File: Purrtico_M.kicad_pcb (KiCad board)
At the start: 2 copper layers, 100 x 60 mm, 123 parts, among them J1 Conn_02x05_Odd_Even, J2 Conn_01x02, J4 Conn_01x02, U1 OPA1679, U2 OPA1679, U3 OPA1679

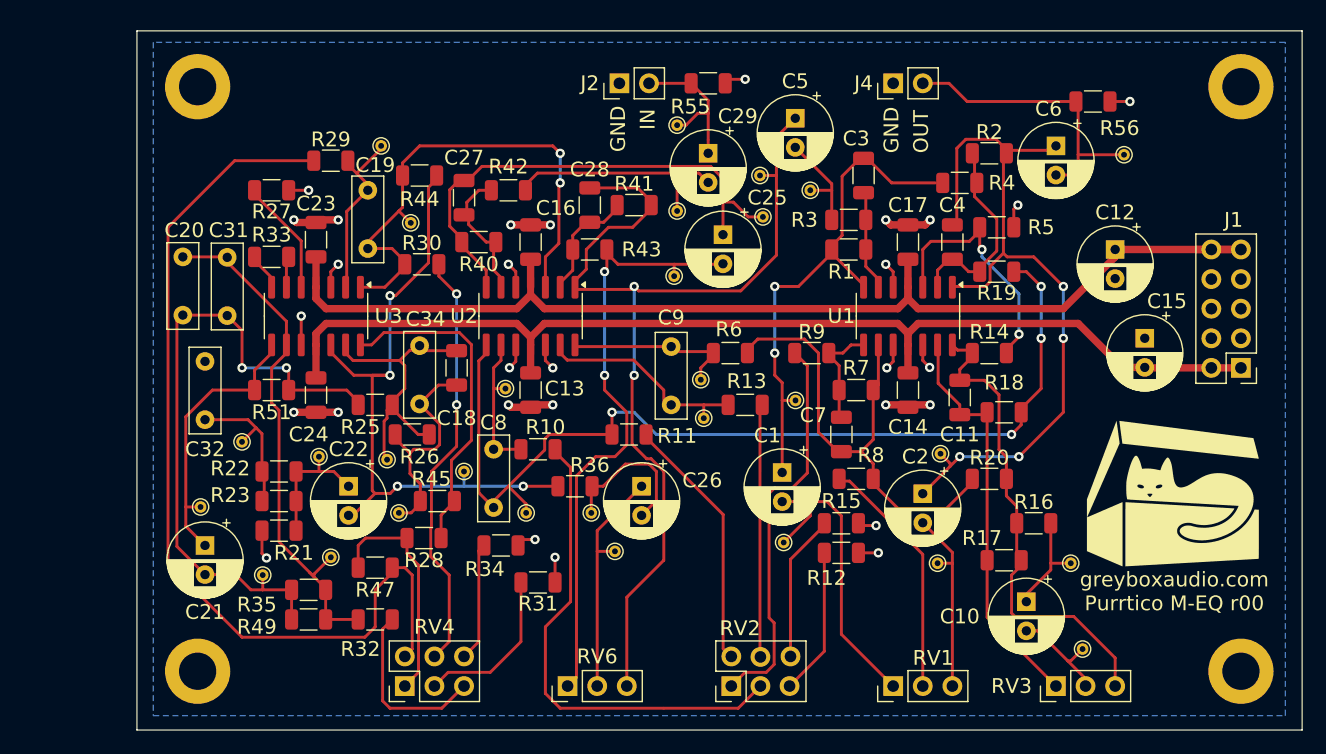
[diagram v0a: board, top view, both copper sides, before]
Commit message: first update after testing
shelving circuit not working for whatever reason :/
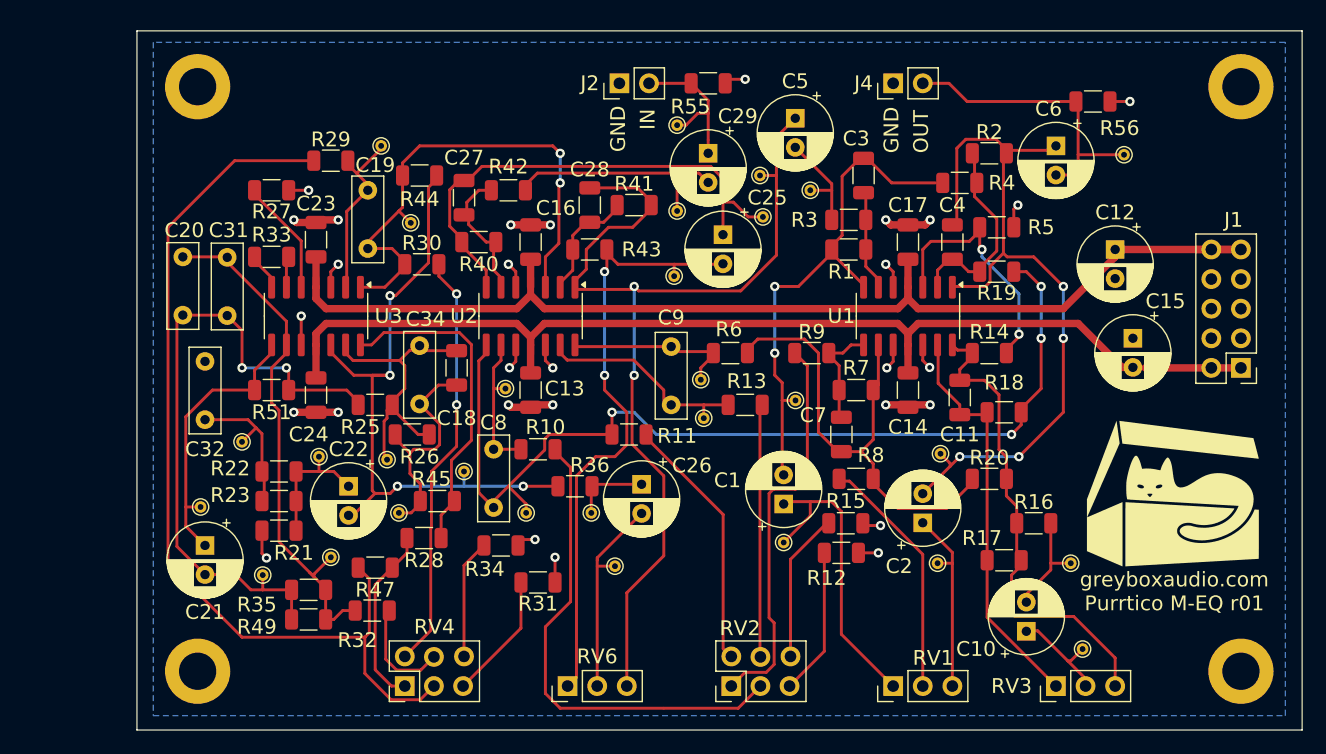
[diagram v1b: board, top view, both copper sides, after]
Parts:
- C8, C9: value 5n6 -> 56n
- RV1, RV6: value 4k7 -> 5k
- moved C1 2.71 mm to (143.0, 70.1), turned to 90 degrees
- moved C10 2.54 mm to (163.8, 81.0), turned to 90 degrees
- moved C2 2.50 mm to (154.9, 71.7), turned to 90 degrees
- moved TP5 1.27 mm to (128.5, 75.4)
- moved C15 1.02 mm to (173.0, 55.9)
- moved R32 0.80 mm to (107.7, 79.2)
- moved R15 0.38 mm to (148.3, 71.8)
- moved C26 0.17 mm to (130.8, 68.4)
- turned R47 to 0 degrees
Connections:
- C3 pad 2: Net-(C1-Pad1) -> Net-(C1-Pad2)
- C4 pad 2: Net-(C2-Pad1) -> Net-(C2-Pad2)
- C6 pad 1: Net-(C2-Pad1) -> Net-(C2-Pad2)
- R1 pad 2: Net-(C1-Pad1) -> Net-(C1-Pad2)
- R16 pad 2: Net-(C10-Pad1) -> Net-(C10-Pad2)
- R2 pad 2: Net-(C2-Pad1) -> Net-(C2-Pad2)
- R36 pad 2: Net-(C26-Pad2) -> Net-(C26-Pad1)
- R4 pad 1: Net-(C1-Pad1) -> Net-(C1-Pad2)
- RV1 pad 1: Net-(C1-Pad2) -> Net-(C1-Pad1)
- RV1 pad 3: Net-(C2-Pad2) -> Net-(C2-Pad1)
- RV3 pad 2: Net-(C10-Pad2) -> Net-(C10-Pad1)
- RV6 pad 2: Net-(C26-Pad1) -> Net-(C26-Pad2)
- TP10 pad 1: Net-(C1-Pad2) -> Net-(C1-Pad1)
- TP11 pad 1: Net-(C2-Pad2) -> Net-(C2-Pad1)
- TP12 pad 1: Net-(C2-Pad1) -> Net-(C2-Pad2)
- TP18 pad 1: Net-(C10-Pad2) -> Net-(C10-Pad1)
- TP19 pad 1: Net-(C10-Pad1) -> Net-(C10-Pad2)
- TP5 pad 1: Net-(C26-Pad1) -> Net-(C26-Pad2)
- TP6 pad 1: Net-(C26-Pad2) -> Net-(C26-Pad1)
- TP9 pad 1: Net-(C1-Pad1) -> Net-(C1-Pad2)
- U1 pad 1: Net-(C2-Pad1) -> Net-(C2-Pad2)
- U1 pad 7: Net-(C1-Pad1) -> Net-(C1-Pad2)
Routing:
- net Net-(C2-Pad2): track 16.3 -> 62.8 mm, vias 0 -> 4
- net Net-(C2-Pad1): track 62.8 -> 16.3 mm, vias 4 -> 0
- net Net-(C1-Pad2): track 26.5 -> 42.3 mm, vias 0 -> 2
- net Net-(C1-Pad1): track 42.3 -> 26.7 mm, vias 2 -> 0
- net Net-(C26-Pad1): track 20.2 -> 6.63 mm
- net Net-(R32-Pad2): track 15.4 -> 9.30 mm
- net Net-(C26-Pad2): track 13.5 -> 18.3 mm
- net Net-(R28-Pad1): track 20.0 -> 15.6 mm
- net Net-(R31-Pad2): track 14.1 -> 10.9 mm
- net Net-(R29-Pad1): track 78.9 -> 80.2 mm
- net -15V: track 93.2 -> 92.2 mm
- net Net-(C10-Pad2): track 8.47 -> 9.31 mm
- net Net-(C10-Pad1): track 9.31 -> 8.47 mm
- net Net-(R34-Pad2): track 10.2 -> 10.9 mm
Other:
- board text added: "greyboxaudio.com Purrtico M-EQ r01"
- board text removed: "greyboxaudio.com Purrtico M-EQ r00"

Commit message: update schematic
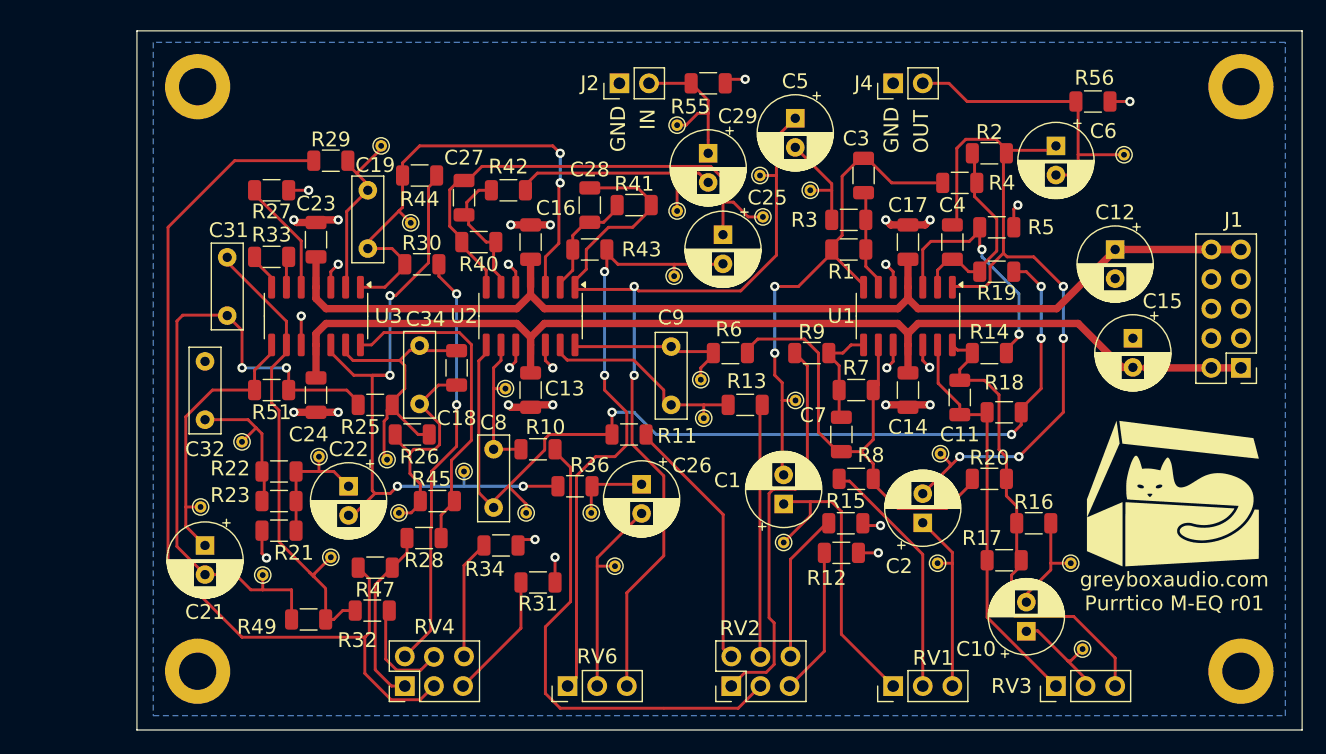
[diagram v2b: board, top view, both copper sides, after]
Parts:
- removed C20: 470n, Capacitor_THT:C_Rect_L7.2mm_W2.5mm_P5.00mm_FKS2_FKP2_MKS2_MKP2
- removed R35: 1M, Resistor_SMD:R_1206_3216Metric
- C31: value 470n -> 4n7
- R12, R15: value 390R -> 2k7
- R28, R30: value 100R -> 3k9
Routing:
- net Net-(U3C--): track 43.8 -> 40.0 mm
- net Net-(C10-Pad2): track 9.31 -> 8.68 mm
- net Net-(R34-Pad2): track 10.9 -> 10.2 mm

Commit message: update pcb
added 470p cap as MLCC, removed two mounting holes to create space for wider potentiometer spacing, swapped rows of RV6 to enable the use of a single gang potentiometer for the high shelf
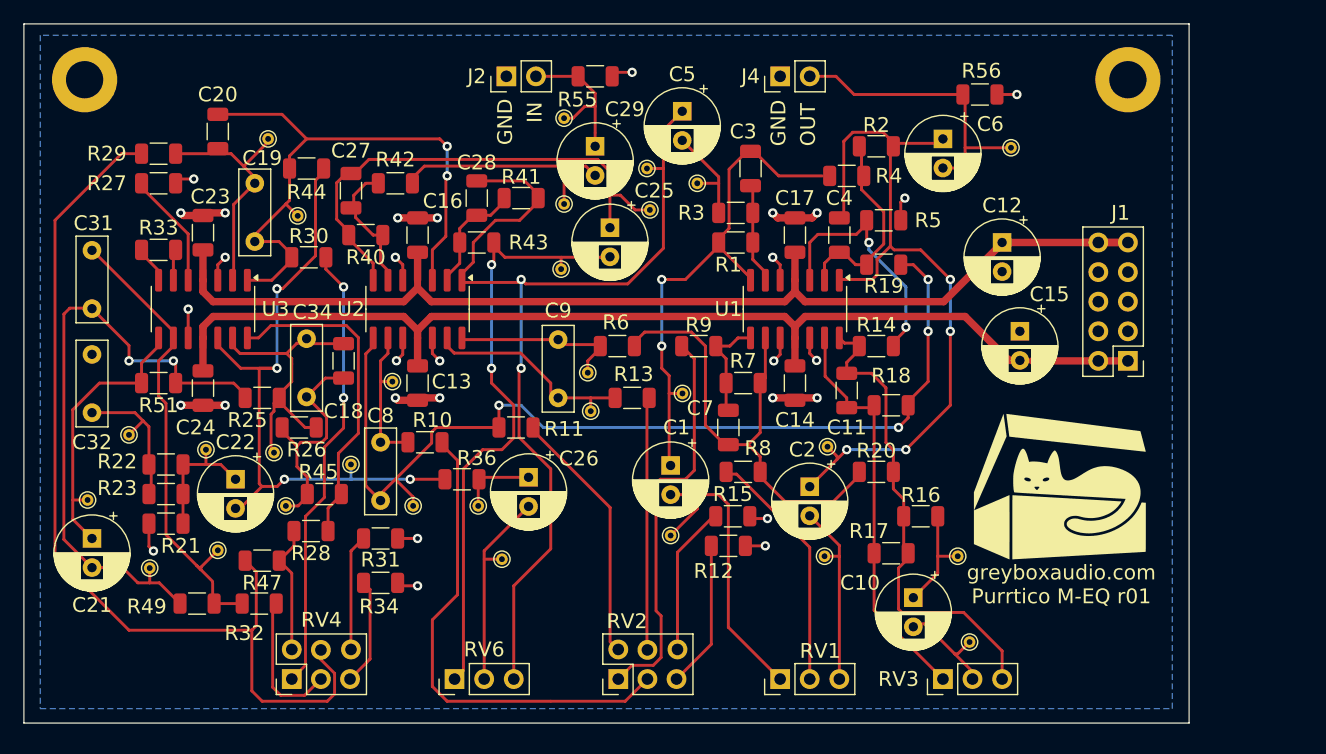
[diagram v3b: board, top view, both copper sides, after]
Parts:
- removed H3, H4: MountingHole, MountingHole:MountingHole_3.2mm_M3_DIN965_Pad
- added C20: 470p, Capacitor_SMD:C_1206_3216Metric, F.Cu at (94.4, 38.1)
- moved R29 14.8 mm to (89.4, 40.0)
- moved R31 14.0 mm to (108.4, 73.1)
- moved C31 11.6 mm to (83.6, 48.3)
- moved R34 10.8 mm to (108.4, 76.9)
- moved C1 10.2 mm to (133.3, 66.8), turned to -90 degrees
- moved C2 10.2 mm to (145.2, 68.6), turned to -90 degrees
- moved C10 10.1 mm to (154.1, 78.1), turned to -90 degrees
- moved C11 9.72 mm to (148.4, 60.4)
- moved C3 9.72 mm to (140.2, 41.3)
- moved C6 9.72 mm to (156.7, 38.8)
- moved C7 9.72 mm to (138.3, 63.5)
- moved H2 9.72 mm to (172.5, 33.7)
- moved J1 9.72 mm to (172.5, 57.8)
- moved J4 9.72 mm to (142.7, 33.4)
- moved R1 9.72 mm to (138.9, 47.7)
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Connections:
- C3 pad 2: Net-(C1-Pad2) -> Net-(C1-Pad1)
- C4 pad 2: Net-(C2-Pad2) -> Net-(C2-Pad1)
- C6 pad 1: Net-(C2-Pad2) -> Net-(C2-Pad1)
- R1 pad 2: Net-(C1-Pad2) -> Net-(C1-Pad1)
- R16 pad 2: Net-(C10-Pad2) -> Net-(C10-Pad1)
- R2 pad 2: Net-(C2-Pad2) -> Net-(C2-Pad1)
- R4 pad 1: Net-(C1-Pad2) -> Net-(C1-Pad1)
- RV1 pad 1: Net-(C1-Pad1) -> Net-(C1-Pad2)
- RV1 pad 3: Net-(C2-Pad1) -> Net-(C2-Pad2)
- RV3 pad 2: Net-(C10-Pad1) -> Net-(C10-Pad2)
- RV4 pad 1: Net-(R28-Pad1) -> Net-(R30-Pad2)
- RV4 pad 2: Net-(R29-Pad1) -> Net-(R32-Pad2)
- RV4 pad 3: Net-(R31-Pad2) -> Net-(R34-Pad2)
- RV4 pad 4: Net-(R30-Pad2) -> Net-(R28-Pad1)
- RV4 pad 5: Net-(R32-Pad2) -> Net-(R29-Pad1)
- RV4 pad 6: Net-(R34-Pad2) -> Net-(R31-Pad2)
- TP10 pad 1: Net-(C1-Pad1) -> Net-(C1-Pad2)
- TP11 pad 1: Net-(C2-Pad1) -> Net-(C2-Pad2)
- TP12 pad 1: Net-(C2-Pad2) -> Net-(C2-Pad1)
- TP18 pad 1: Net-(C10-Pad1) -> Net-(C10-Pad2)
- TP19 pad 1: Net-(C10-Pad2) -> Net-(C10-Pad1)
- TP9 pad 1: Net-(C1-Pad2) -> Net-(C1-Pad1)
- U1 pad 1: Net-(C2-Pad2) -> Net-(C2-Pad1)
- U1 pad 7: Net-(C1-Pad2) -> Net-(C1-Pad1)
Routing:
- net Net-(C2-Pad2): track 62.8 -> 16.3 mm, vias 4 -> 0
- net Net-(C2-Pad1): track 16.3 -> 62.8 mm, vias 0 -> 4
- net Net-(C1-Pad1): track 26.7 -> 42.3 mm, vias 0 -> 2
- net Net-(C1-Pad2): track 42.3 -> 26.7 mm, vias 2 -> 0
- net Net-(U2A-+): track 44.0 -> 52.5 mm
- net Net-(U3A--): track 14.4 -> 19.6 mm
- net Net-(R28-Pad1): track 15.6 -> 11.1 mm
- net Net-(R32-Pad2): track 8.86 -> 11.9 mm
- net Net-(C21-Pad2): track 56.2 -> 53.4 mm
- net Net-(R30-Pad2): track 36.1 -> 38.7 mm
- net Net-(R29-Pad1): track 80.2 -> 81.9 mm
- net Net-(C10-Pad1): track 8.47 -> 9.57 mm
- net Net-(R34-Pad2): track 10.2 -> 9.20 mm
- net Net-(R31-Pad2): track 10.9 -> 9.97 mm
- net GND: track 56.2 -> 55.2 mm
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
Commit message: update pcb
swapped potentiometer pinouts, increased potentiometer spacing on pcb
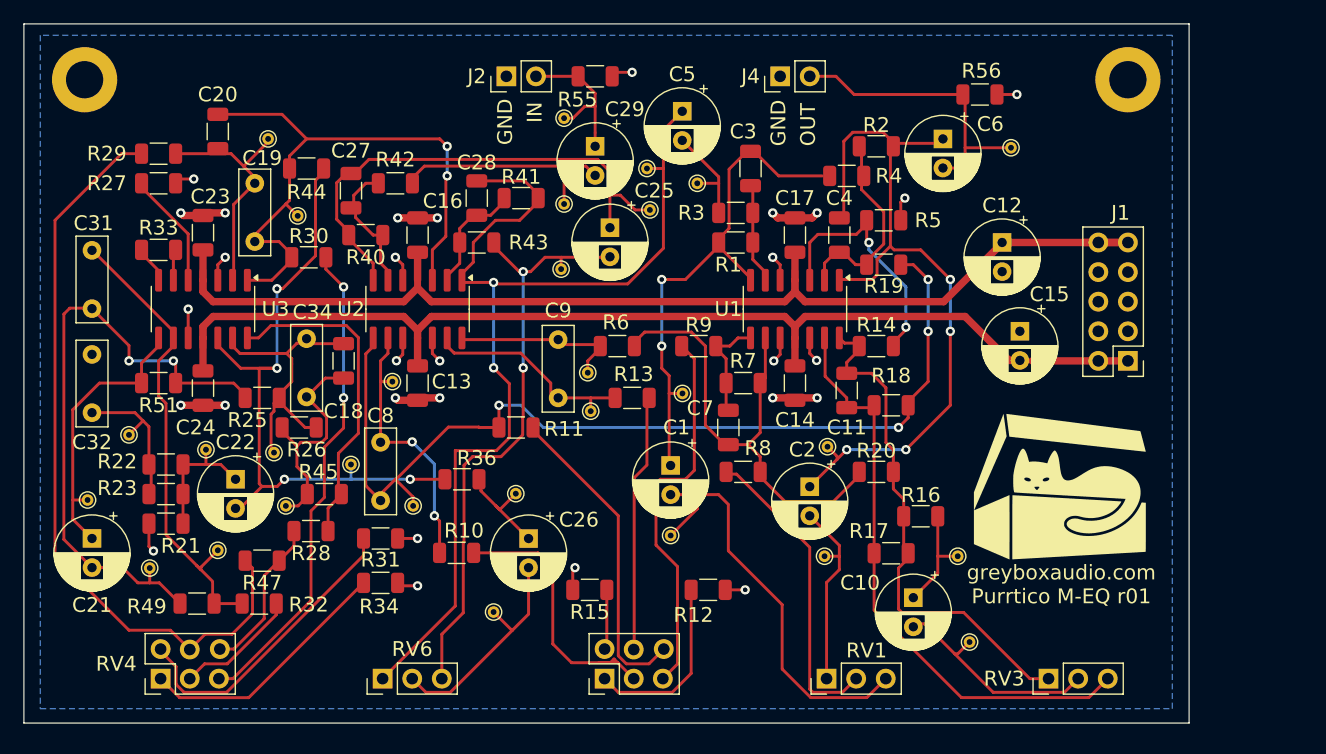
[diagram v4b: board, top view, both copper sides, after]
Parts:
- moved R15 13.8 mm to (126.4, 77.5), turned to 0 degrees
- moved RV4 11.3 mm to (89.5, 85.1)
- moved R10 9.87 mm to (114.9, 74.3)
- moved RV3 9.07 mm to (165.7, 85.1)
- moved RV6 6.18 mm to (108.6, 85.1)
- moved C26 5.25 mm to (121.1, 73.1)
- moved TP5 4.59 mm to (118.1, 79.4)
- moved R12 4.15 mm to (136.5, 77.5)
- moved RV1 3.99 mm to (146.7, 85.1)
- moved TP6 3.39 mm to (120.0, 69.2)
- moved RV2 1.18 mm to (127.6, 85.1)
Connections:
- RV1 pad 1: Net-(C1-Pad2) -> Net-(C2-Pad2)
- RV1 pad 3: Net-(C2-Pad2) -> Net-(C1-Pad2)
- RV2 pad 1: Net-(R9-Pad1) -> Net-(R12-Pad2)
- RV2 pad 3: Net-(R12-Pad2) -> Net-(R9-Pad1)
- RV2 pad 4: Net-(R11-Pad2) -> Net-(R15-Pad2)
- RV2 pad 6: Net-(R15-Pad2) -> Net-(R11-Pad2)
- RV3 pad 1: Net-(U1D--) -> Net-(C11-Pad1)
- RV3 pad 3: Net-(C11-Pad1) -> Net-(U1D--)
- RV4 pad 1: Net-(R30-Pad2) -> Net-(R34-Pad2)
- RV4 pad 3: Net-(R34-Pad2) -> Net-(R30-Pad2)
- RV4 pad 4: Net-(R28-Pad1) -> Net-(R31-Pad2)
- RV4 pad 6: Net-(R31-Pad2) -> Net-(R28-Pad1)
- RV6 pad 1: Net-(C25-Pad2) -> Net-(C28-Pad2)
- RV6 pad 3: Net-(C28-Pad2) -> Net-(C25-Pad2)
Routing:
- net Net-(R10-Pad1): track 41.9 -> 23.9 mm
- net Net-(R29-Pad1): track 81.9 -> 65.0 mm
- net Net-(R31-Pad2): track 9.97 -> 26.1 mm
- net Net-(U1D--): track 34.8 -> 50.3 mm
- net Net-(R34-Pad2): track 9.20 -> 22.2 mm
- net Net-(U2C--): track 12.6 -> 23.9 mm, vias 0 -> 2
- net Net-(C10-Pad2): track 8.47 -> 18.8 mm
- net Net-(C1-Pad2): track 26.7 -> 36.5 mm
- net Net-(R15-Pad2): track 12.4 -> 4.89 mm
- net Net-(R8-Pad1): track 20.7 -> 26.2 mm
- net Net-(R11-Pad2): track 21.8 -> 27.1 mm
- net Net-(C28-Pad2): track 85.1 -> 89.2 mm
- net Net-(R30-Pad2): track 38.7 -> 41.9 mm
- net Net-(C11-Pad1): track 39.3 -> 42.5 mm
- net Net-(R12-Pad2): track 12.7 -> 15.8 mm
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
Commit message: clean up pcb
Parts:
- moved R13 12.8 mm to (128.5, 73.7), turned to 180 degrees
- moved R34 4.15 mm to (106.7, 80.6)
- moved R16 4.11 mm to (156.2, 67.3)
- moved R31 3.78 mm to (108.6, 76.8)
- moved TP19 3.01 mm to (154.9, 74.3)
- moved TP18 2.82 mm to (156.8, 83.8)
- moved C21 2.63 mm to (83.6, 75.7)
- moved R17 2.58 mm to (152.4, 71.8)
- moved R26 2.55 mm to (101.0, 66.0), turned to 0 degrees
- moved TP23 2.44 mm to (100.3, 63.5)
- moved TP10 2.13 mm to (135.3, 73.7)
- moved R28 2.11 mm to (103.6, 74.2)
- moved G*** 1.94 mm to (166.8, 66.7)
- moved R8 1.93 mm to (139.1, 69.2)
- moved TP16 1.81 mm to (83.2, 67.9)
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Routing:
- net Net-(R13-Pad2): track 21.6 -> 10.2 mm
- net Net-(U2D--): track 17.5 -> 28.9 mm
- net Net-(C11-Pad1): track 42.5 -> 48.1 mm
- net Net-(C18-Pad2): track 18.9 -> 13.8 mm
- net Net-(C21-Pad1): track 23.6 -> 27.8 mm
- net Net-(C10-Pad1): track 9.57 -> 13.3 mm
- net Net-(R11-Pad2): track 27.1 -> 23.4 mm
- net Net-(C1-Pad2): track 36.5 -> 33.1 mm
- net Net-(R34-Pad2): track 22.2 -> 19.5 mm
- net Net-(C32-Pad1): track 12.5 -> 9.85 mm
- net Net-(R31-Pad2): track 26.1 -> 23.9 mm
- net Net-(U3D--): track 22.5 -> 20.5 mm
- net Net-(R10-Pad1): track 23.9 -> 22.0 mm
- net Net-(R8-Pad1): track 26.2 -> 24.2 mm
- net Net-(U1C--): track 40.3 -> 42.2 mm
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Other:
- board text added: "greyboxaudio.com Purrtico M r01"
- board text removed: "greyboxaudio.com Purrtico M-EQ r01"

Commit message: update pcb
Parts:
- moved H1 1.48 mm to (83.8, 34.9)
- moved H2 1.32 mm to (172.1, 34.9)
- moved C14 0.06 mm to (144.0, 59.7)
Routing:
- net GND: track 57.4 -> 60.3 mm

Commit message: tweak LF EQ
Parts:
- C19: value 68n -> 100n
- C32: value 680n -> 1u
- R23: value 2k2 -> 1k
- R28, R30: value 3k9 -> 100R
- moved R22 2.63 mm to (89.9, 69.3)
- moved R23 2.45 mm to (89.9, 66.8)
- moved R21 0.12 mm to (89.9, 71.9)
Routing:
- net GND: track 60.3 -> 60.8 mm

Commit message: tuned low shelf
tuned the low shelf so that it closely matches the 5033
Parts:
- C19: value 100n -> 150n
- R23: value 1k -> 750R
